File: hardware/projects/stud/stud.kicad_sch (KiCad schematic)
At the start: 4 parts, among them IC1 R7KA8M2JFLCAC#UC0, IC2 IS42S32160F-7BLI, U2 TAC5242

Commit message: add a buck converter
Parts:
- added U1: TPS629210DRLR, vendor:SOT50P160X60-8N, symbol vendor:TPS629210DRLR
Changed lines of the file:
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@@
+	)
+	(symbol
+		(lib_id "vendor:TPS629210DRLR")
+		(at 251.46 161.29 0)
+		(unit 1)
+		(body_style 1)
+		(exclude_from_sim no)
+		(in_bom yes)
+		(on_board yes)
+		(in_pos_files yes)
+		(dnp no)
+		(fields_autoplaced yes)
+		(property "Reference" "U1"
+			(at 251.46 140.97 0)
+			(show_name no)
+			(do_not_autoplace no)
+			(effects
+				(font
+					(size 1.27 1.27)
+				)
+			)
+		)
+		(property "Value" "TPS629210DRLR"
+			(at 251.46 143.51 0)
+			(show_name no)
+			(do_not_autoplace no)
+			(effects
+				(font
+					(size 1.27 1.27)
+				)
+			)
+		)
+		(property "Footprint" "vendor:SOT50P160X60-8N"
+			(at 251.46 161.29 0)
+			(hide yes)
+			(show_name no)
+			(do_not_autoplace no)
+			(effects
+				(font
+					(size 1.27 1.27)
+				)
+				(justify bottom)
+			)
+		)
+		(property "Datasheet" ""
+			(at 251.46 161.29 0)
+			(hide yes)
+			(show_name no)
+			(do_not_autoplace no)
+			(effects
+				(font
+					(size 1.27 1.27)
+				)
+			)
+		)
+		(property "Description" ""
+			(at 251.46 161.29 0)
+			(hide yes)
+			(show_name no)
+			(do_not_autoplace no)
+			(effects
+				(font
+					(size 1.27 1.27)
+				)
+			)
+		)
+		(property "PARTREV" "B"
+			(at 251.46 161.29 0)
+			(hide yes)
+			(show_name no)
+			(do_not_autoplace no)
+			(effects
+				(font
+					(size 1.27 1.27)
+				)
+				(justify bottom)
+			)
+		)
+		(property "STANDARD" "IPC-7351B"
+			(at 251.46 161.29 0)
+			(hide yes)
+			(show_name no)
+			(do_not_autoplace no)
+			(effects
+				(font
+					(size 1.27 1.27)
+				)
+				(justify bottom)
+			)
+		)
+		(property "MAXIMUM_PACKAGE_HEIGHT" "0.6 mm"
+			(at 251.46 161.29 0)
+			(hide yes)
+			(show_name no)
+			(do_not_autoplace no)
+			(effects
+				(font
+					(size 1.27 1.27)
+				)
+				(justify bottom)
+			)
+		)
+		(property "MANUFACTURER" "Texas Instruments"
+			(at 251.46 161.29 0)
+			(hide yes)
+			(show_name no)
+			(do_not_autoplace no)
+			(effects
+				(font
+					(size 1.27 1.27)
+				)
+				(justify bottom)
+			)
+		)
+		(pin "5"
+		)
+		(pin "7"
+		)
+		(pin "6"
+		)
+		(pin "3"
+		)
+		(pin "8"
+		)
+		(pin "4"
+		)
+		(pin "2"
+		)
+		(pin "1"
+		)
+		(instances
+			(project "stud"
+				(path "/5a440a9e-b660-4605-bd2b-6a991cc5b149"
+					(reference "U1")
+					(unit 1)
+				)
+			)
+		)
 	)
 	(symbol

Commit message: add a 25 MHz crystal
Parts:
- added Y1: X1G0044510004, custom:SG5032CAN, symbol custom:CrystalOsc_X1G0044510004
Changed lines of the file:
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@@
+	)
+	(symbol
+		(lib_id "custom:CrystalOsc_X1G0044510004")
+		(at 152.4 158.75 0)
+		(unit 1)
+		(body_style 1)
+		(exclude_from_sim no)
+		(in_bom yes)
+		(on_board yes)
+		(in_pos_files yes)
+		(dnp no)
+		(fields_autoplaced yes)
+		(property "Reference" "Y1"
+			(at 152.4 149.86 0)
+			(show_name no)
+			(do_not_autoplace no)
+			(effects
+				(font
+					(size 1.27 1.27)
+				)
+			)
+		)
+		(property "Value" "X1G0044510004"
+			(at 152.4 152.4 0)
+			(show_name no)
+			(do_not_autoplace no)
+			(effects
+				(font
+					(size 1.27 1.27)
+				)
+			)
+		)
+		(property "Footprint" "custom:SG5032CAN"
+			(at 152.146 152.4 0)
+			(hide yes)
+			(show_name no)
+			(do_not_autoplace no)
+			(effects
+				(font
+					(size 1.27 1.27)
+				)
+			)
+		)
+		(property "Datasheet" ""
+			(at 152.4 158.75 0)
+			(hide yes)
+			(show_name no)
+			(do_not_autoplace no)
+			(effects
+				(font
+					(size 1.27 1.27)
+				)
+			)
+		)
+		(property "Description" ""
+			(at 152.4 158.75 0)
+			(hide yes)
+			(show_name no)
+			(do_not_autoplace no)
+			(effects
+				(font
+					(size 1.27 1.27)
+				)
+			)
+		)
+		(pin "4"
+		)
+		(pin "1"
+		)
+		(pin "2"
+		)
+		(pin "3"
+		)
+		(instances
+			(project "stud"
+				(path "/5a440a9e-b660-4605-bd2b-6a991cc5b149"
+					(reference "Y1")
+					(unit 1)
+				)
+			)
+		)
 	)
 	(symbol

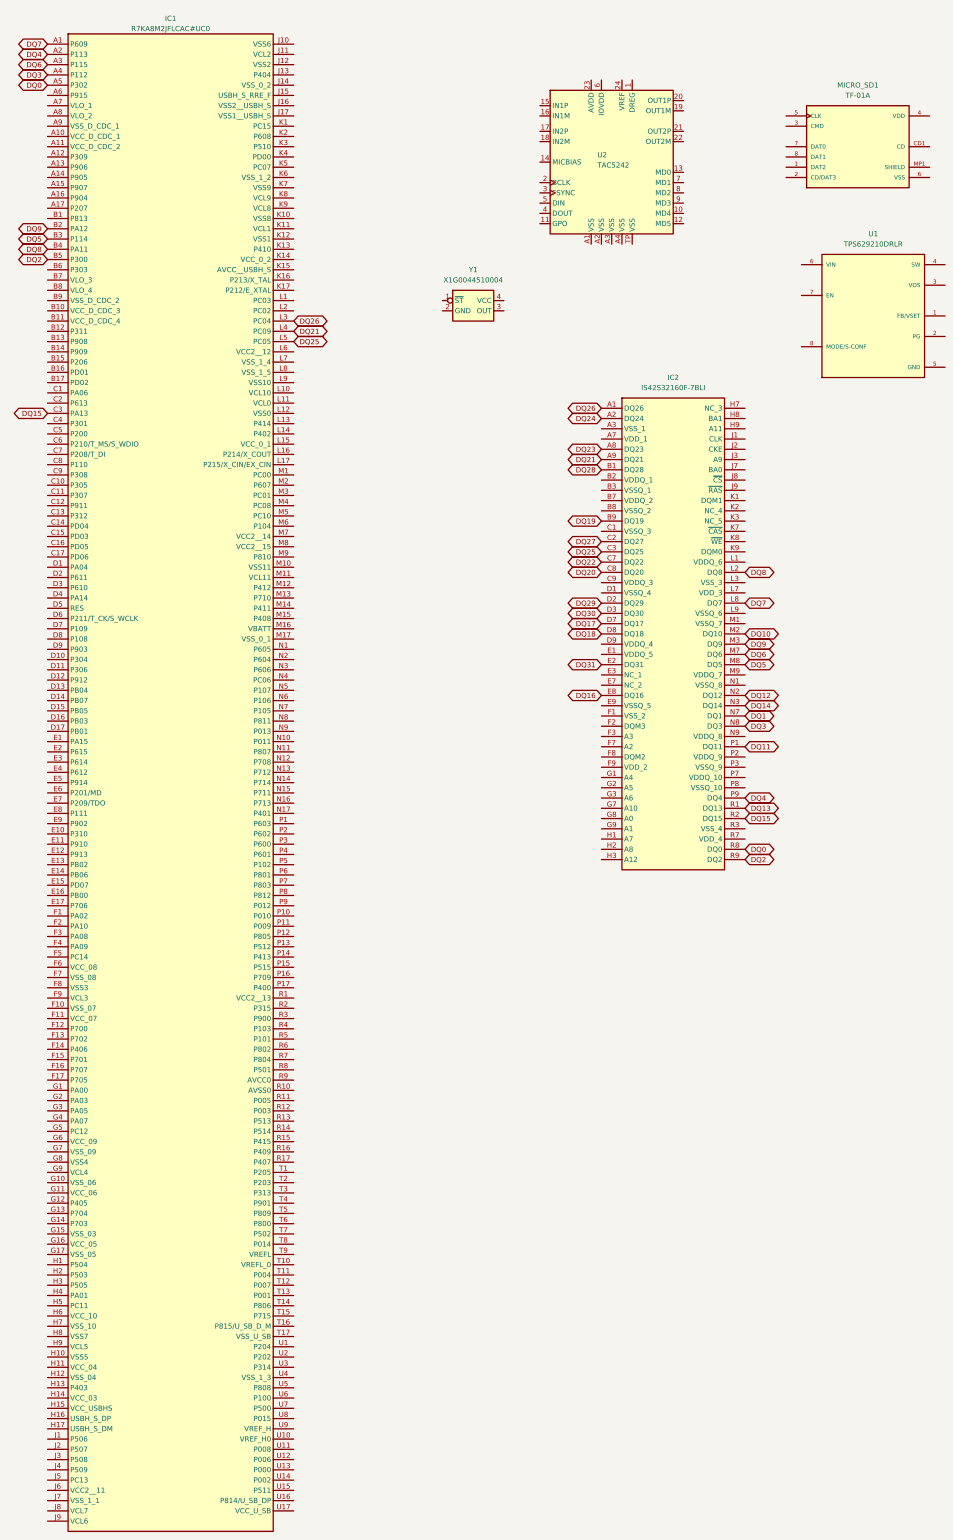
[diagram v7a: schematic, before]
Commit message: label signal lines for SDRAM
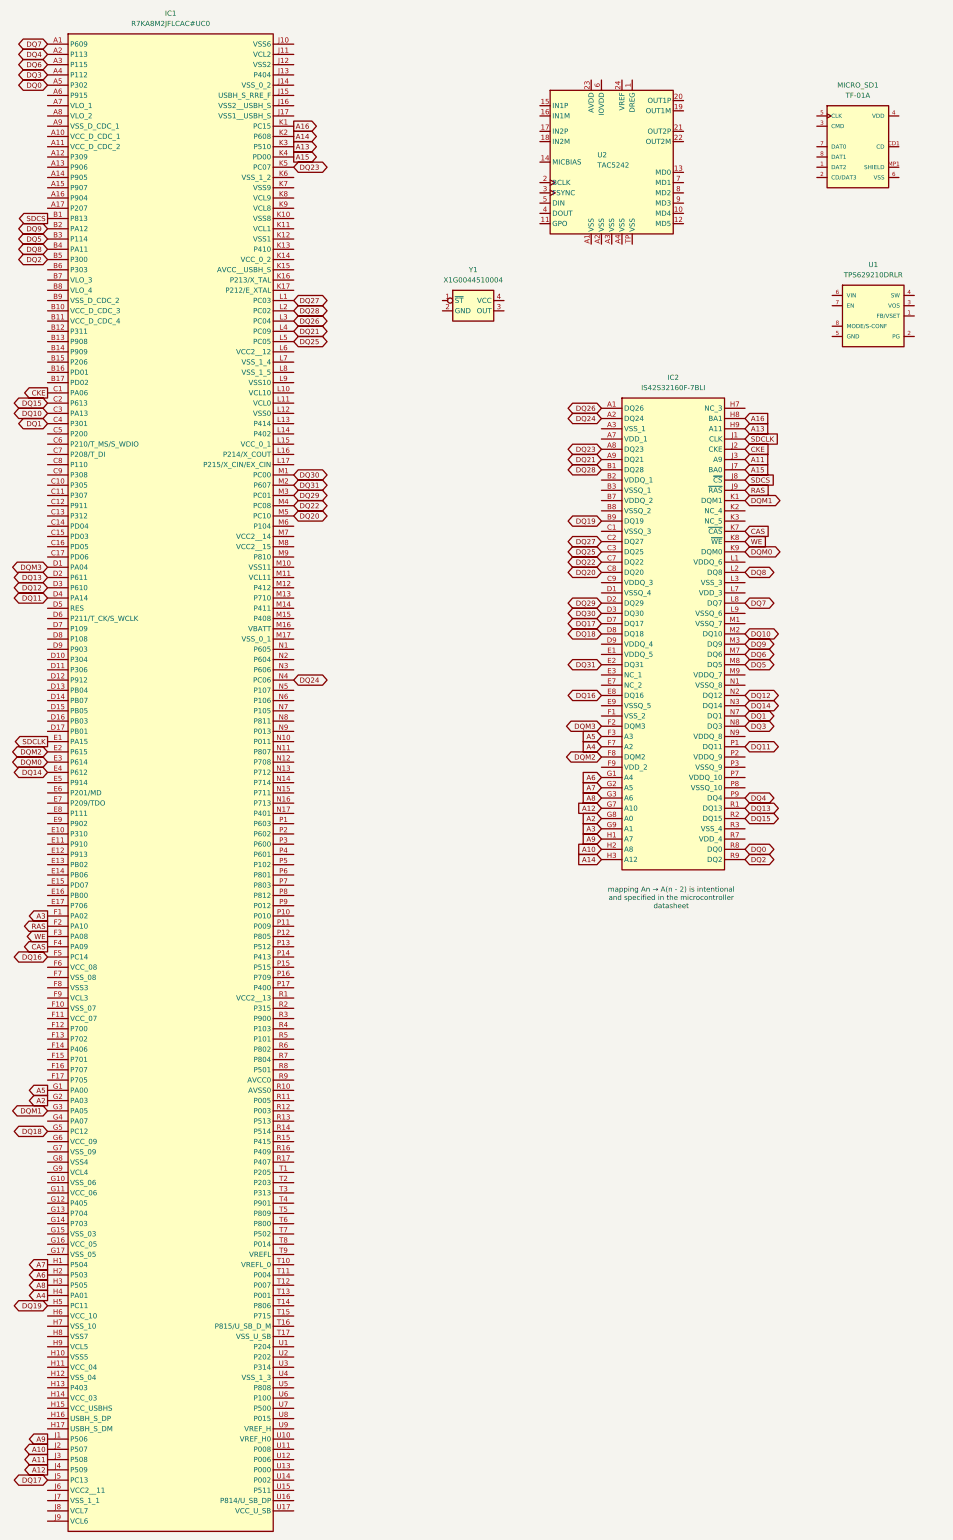
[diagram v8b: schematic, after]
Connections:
- net DQ1: now also IC1.C4 (P301)
- net DQ10: now also IC1.C3 (PA13)
- net DQ11: now also IC1.D4 (PA14)
- net DQ12: now also IC1.D3 (P610)
- net DQ13: now also IC1.D2 (P611)
- net DQ14: now also IC1.E4 (P612)
- net DQ15: now also IC1.C2 (P613); no longer IC1.C3 (PA13)
- net DQ16: now also IC1.F5 (PC14)
- net DQ17: now also IC1.J5 (PC13)
- net DQ18: now also IC1.G5 (PC12)
- net DQ19: now also IC1.H5 (PC11)
- net DQ20: now also IC1.M5 (PC10)
- net DQ22: now also IC1.M4 (PC08)
- net DQ23: now also IC1.K5 (PC07)
- net DQ24: now also IC1.N4 (PC06)
- net DQ27: now also IC1.L1 (PC03)
- net DQ28: now also IC1.L2 (PC02)
- net DQ29: now also IC1.M3 (PC01)
- net DQ30: now also IC1.M1 (PC00)
- net DQ31: now also IC1.M2 (P607)
- net SHIELD: no longer MICRO_SD1.MP1 (SHIELD)
- net SDCS: now reaches IC1.B1 (P813)
- net SDCS: now also IC2.J8 (~{CS})
- net CKE: now reaches IC1.C1 (PA06)
- net CKE: now also IC2.J2 (CKE)
- net DQM3: now reaches IC1.D1 (PA04)
- net DQM3: now also IC2.F2 (DQM3)
- net SDCLK: now reaches IC1.E1 (PA15)
- net SDCLK: now also IC2.J1 (CLK)
- net DQM2: now reaches IC1.E2 (P615)
- net DQM2: now also IC2.F8 (DQM2)
- net DQM0: now reaches IC1.E3 (P614)
- net DQM0: now also IC2.K9 (DQM0)
- net A3: now reaches IC1.F1 (PA02)
- net A3: now also IC2.G9 (A1)
- net RAS: now reaches IC1.F2 (PA10)
- net RAS: now also IC2.J9 (~{RAS})
- net WE: now reaches IC1.F3 (PA08)
- net WE: now also IC2.K8 (~{WE})
- net CAS: now reaches IC1.F4 (PA09)
- net CAS: now also IC2.K7 (~{CAS})
- net A5: now reaches IC1.G1 (PA00)
- net A5: now also IC2.F3 (A3)
- net A2: now reaches IC1.G2 (PA03)
- net A2: now also IC2.G8 (A0)
- net DQM1: now reaches IC1.G3 (PA05)
- net DQM1: now also IC2.K1 (DQM1)
- net A7: now reaches IC1.H1 (P504)
- net A7: now also IC2.G2 (A5)
- net A6: now reaches IC1.H2 (P503)
- net A6: now also IC2.G1 (A4)
- net A8: now reaches IC1.H3 (P505)
- net A8: now also IC2.G3 (A6)
- net A4: now reaches IC1.H4 (PA01)
- net A4: now also IC2.F7 (A2)
- net A9: now reaches IC1.J1 (P506)
- net A9: now also IC2.H1 (A7)
- net A10: now reaches IC1.J2 (P507)
- net A10: now also IC2.H2 (A8)
- net A11: now reaches IC1.J3 (P508)
- net A11: now also IC2.J3 (A9)
- net A12: now reaches IC1.J4 (P509)
- net A12: now also IC2.G7 (A10)
- net A16: now reaches IC1.K1 (PC15)
- net A16: now also IC2.H8 (BA1)
- net A14: now reaches IC1.K2 (P608)
- net A14: now also IC2.H3 (A12)
- net A13: now reaches IC1.K3 (P510)
- net A13: now also IC2.H9 (A11)
- net A15: now reaches IC1.K4 (PD00)
- net A15: now also IC2.J7 (BA0)
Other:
- note added: "mapping An → A(n - 2) is intentional and specified in the microcontroller datasheet"
